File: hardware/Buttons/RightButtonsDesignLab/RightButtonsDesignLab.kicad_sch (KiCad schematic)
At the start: 5 parts, among them J1 Conn_01x03, J2 Conn_01x01, SW1 SW_Push, SW2 SW_Push, SW3 SW_Push

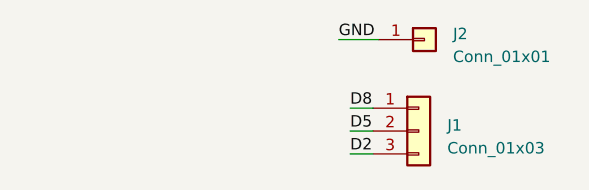
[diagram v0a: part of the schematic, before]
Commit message: BOM of buttons generated
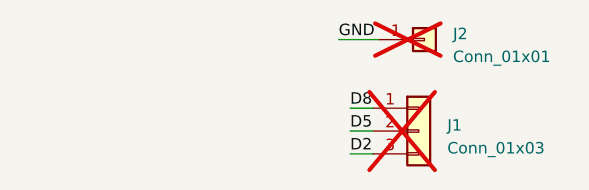
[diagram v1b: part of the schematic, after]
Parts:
- J1, J2: now not fitted
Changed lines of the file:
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@@
   )
   (symbol (lib_id "Connector_Generic:Conn_01x03") (at 189.23 33.655 0) (unit 1)
-    (in_bom yes) (on_board yes) (dnp no) (fields_autoplaced)
+    (in_bom yes) (on_board yes) (dnp yes) (fields_autoplaced)
     (property "Reference" "J1" (at 192.405 33.02 0)
       (effects (font (size 1.27 1.27)) (justify left))
@@
   )
   (symbol (lib_id "Connector_Generic:Conn_01x01") (at 189.865 23.495 0) (unit 1)
-    (in_bom yes) (on_board yes) (dnp no) (fields_autoplaced)
+    (in_bom yes) (on_board yes) (dnp yes) (fields_autoplaced)
     (property "Reference" "J2" (at 193.04 22.86 0)
       (effects (font (size 1.27 1.27)) (justify left))

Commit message: Update all PCB and schematics
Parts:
- removed J1: Conn_01x03, Connector_PinHeader_2.54mm:PinHeader_1x03_P2.54mm_Vertical, symbol Connector_Generic:Conn_01x03
- removed J2: Conn_01x01, Connector_PinHeader_2.54mm:PinHeader_1x01_P2.54mm_Vertical, symbol Connector_Generic:Conn_01x01
- added J1: Conn_01x04, Design:JST_S4B-PH-K-S_LF__SN_, symbol Connector_Generic:Conn_01x04
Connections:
- net D2: now also J1.3 (Pin_3)
- net D5: now also J1.2 (Pin_2)
- net D8: now also J1.1 (Pin_1)
- net GND: now also J1.4 (Pin_4)
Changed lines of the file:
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@@
 (kicad_sch (version 20230121) (generator eeschema)
   (paper "A4")
-  (wire (pts (xy 180.34 23.495) (xy 184.785 23.495))
+  (wire (pts (xy 27.94 37.465) (xy 34.29 37.465))
     (stroke (width 0) (type default))
   )
-  (wire (pts (xy 27.94 37.465) (xy 34.29 37.465))
+  (wire (pts (xy 181.61 38.1) (xy 185.42 38.1))
+    (stroke (width 0) (type default))
+  )
+  (wire (pts (xy 181.61 33.02) (xy 185.42 33.02))
     (stroke (width 0) (type default))
   )
@@
     (stroke (width 0) (type default))
   )
-  (wire (pts (xy 181.61 33.655) (xy 184.15 33.655))
+  (wire (pts (xy 69.215 37.465) (xy 75.565 37.465))
     (stroke (width 0) (type default))
   )
-  (wire (pts (xy 69.215 37.465) (xy 75.565 37.465))
+  (wire (pts (xy 181.61 35.56) (xy 185.42 35.56))
     (stroke (width 0) (type default))
   )
@@
     (stroke (width 0) (type default))
   )
-  (wire (pts (xy 181.61 31.115) (xy 184.15 31.115))
-    (stroke (width 0) (type default))
-  )
-  (wire (pts (xy 181.61 36.195) (xy 184.15 36.195))
+  (wire (pts (xy 181.61 40.64) (xy 185.42 40.64))
     (stroke (width 0) (type default))
   )
@@
     (effects (font (size 1.27 1.27)) (justify left bottom))
   )
-  (label "GND" (at 27.94 37.465 0) (fields_autoplaced)
+  (label "D2" (at 181.61 38.1 0) (fields_autoplaced)
     (effects (font (size 1.27 1.27)) (justify left bottom))
   )
-  (label "GND" (at 180.34 23.495 0) (fields_autoplaced)
+  (label "D5" (at 181.61 35.56 0) (fields_autoplaced)
     (effects (font (size 1.27 1.27)) (justify left bottom))
   )
-  (label "D2" (at 181.61 36.195 0) (fields_autoplaced)
+  (label "GND" (at 27.94 37.465 0) (fields_autoplaced)
     (effects (font (size 1.27 1.27)) (justify left bottom))
   )
@@
     (effects (font (size 1.27 1.27)) (justify left bottom))
   )
-  (label "D5" (at 181.61 33.655 0) (fields_autoplaced)
-    (effects (font (size 1.27 1.27)) (justify left bottom))
-  )
   (label "D2" (at 46.99 37.465 0) (fields_autoplaced)
     (effects (font (size 1.27 1.27)) (justify left bottom))
   )
-  (label "D8" (at 181.61 31.115 0) (fields_autoplaced)
+  (label "D8" (at 125.095 37.465 0) (fields_autoplaced)
     (effects (font (size 1.27 1.27)) (justify left bottom))
   )
-  (label "D8" (at 125.095 37.465 0) (fields_autoplaced)
+  (label "D8" (at 181.61 33.02 0) (fields_autoplaced)
+    (effects (font (size 1.27 1.27)) (justify left bottom))
+  )
+  (label "GND" (at 181.61 40.64 0) (fields_autoplaced)
     (effects (font (size 1.27 1.27)) (justify left bottom))
   )
@@
     )
   )
-  (symbol (lib_id "Connector_Generic:Conn_01x03") (at 189.23 33.655 0) (unit 1)
-    (in_bom yes) (on_board yes) (dnp yes) (fields_autoplaced)
-    (property "Reference" "J1" (at 192.405 33.02 0)
-      (effects (font (size 1.27 1.27)) (justify left))
+  (symbol (lib_id "Connector_Generic:Conn_01x04") (at 190.5 35.56 0) (unit 1)
+    (in_bom yes) (on_board yes) (dnp no)
+    (property "Reference" "J1" (at 190.5 46.355 0)
+      (effects (font (size 1.27 1.27)))
     )
-    (property "Value" "Conn_01x03" (at 192.405 35.56 0)
-      (effects (font (size 1.27 1.27)) (justify left))
+    (property "Value" "Conn_01x04" (at 190.5 43.815 0)
+      (effects (font (size 1.27 1.27)))
     )
-    (property "Footprint" "Connector_PinHeader_2.54mm:PinHeader_1x03_P2.54mm_Vertical" (at 189.23 33.655 0)
+    (property "Footprint" "Design:JST_S4B-PH-K-S_LF__SN_" (at 190.5 35.56 0)
       (effects (font (size 1.27 1.27)) hide)
     )
-    (property "Datasheet" "~" (at 189.23 33.655 0)
+    (property "Datasheet" "https://datasheet.lcsc.com/lcsc/2304140030_JST-S4B-PH-K-S-LF-SN_C157926.pdf" (at 190.5 35.56 0)
+      (effects (font (size 1.27 1.27)) hide)
+    )
+    (property "LCSC#" "C157926" (at 190.5 35.56 0)
       (effects (font (size 1.27 1.27)) hide)
     )
@@
     (pin "2")
     (pin "3")
+    (pin "4")
     (instances
       (project "RightButtonsDesignLab"
@@
         )
       )
-      (project "ButtonDesignLab"
-        (path "/e63e39d7-6ac0-4ffd-8aa3-1841a4541b55"
-          (reference "J2") (unit 1)
-        )
-      )
-    )
-  )
-  (symbol (lib_id "Connector_Generic:Conn_01x01") (at 189.865 23.495 0) (unit 1)
-    (in_bom yes) (on_board yes) (dnp yes) (fields_autoplaced)
-    (property "Reference" "J2" (at 193.04 22.86 0)
-      (effects (font (size 1.27 1.27)) (justify left))
-    )
-    (property "Value" "Conn_01x01" (at 193.04 25.4 0)
-      (effects (font (size 1.27 1.27)) (justify left))
-    )
-    (property "Footprint" "Connector_PinHeader_2.54mm:PinHeader_1x01_P2.54mm_Vertical" (at 189.865 23.495 0)
-      (effects (font (size 1.27 1.27)) hide)
-    )
-    (property "Datasheet" "~" (at 189.865 23.495 0)
-      (effects (font (size 1.27 1.27)) hide)
-    )
-    (pin "1")
-    (instances
-      (project "RightButtonsDesignLab"
-        (path "/d8ab91b7-7f4a-4c3a-afb3-beb7d8cda53a"
-          (reference "J2") (unit 1)
-        )
-      )
-      (project "ButtonDesignLab"
-        (path "/e63e39d7-6ac0-4ffd-8aa3-1841a4541b55"
-          (reference "J7") (unit 1)
-        )
-      )

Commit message: Update PCB
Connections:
- net D2: now also J1.2 (Pin_2); no longer J1.3 (Pin_3)
- net D5: now also J1.3 (Pin_3); no longer J1.2 (Pin_2)
- net D8: now also J1.4 (Pin_4); no longer J1.1 (Pin_1)
- net GND: now also J1.1 (Pin_1); no longer J1.4 (Pin_4)
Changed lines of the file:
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@@
     )
   )
-  (symbol (lib_id "Connector_Generic:Conn_01x04") (at 190.5 35.56 0) (unit 1)
+  (symbol (lib_id "Connector_Generic:Conn_01x04") (at 190.5 38.1 0) (mirror x) (unit 1)
     (in_bom yes) (on_board yes) (dnp no)
-    (property "Reference" "J1" (at 190.5 46.355 0)
+    (property "Reference" "J1" (at 190.5 27.305 0)
       (effects (font (size 1.27 1.27)))
     )
-    (property "Value" "Conn_01x04" (at 190.5 43.815 0)
+    (property "Value" "Conn_01x04" (at 190.5 29.845 0)
       (effects (font (size 1.27 1.27)))
     )
-    (property "Footprint" "Design:JST_S4B-PH-K-S_LF__SN_" (at 190.5 35.56 0)
+    (property "Footprint" "Design:JST_S4B-PH-K-S_LF__SN_" (at 190.5 38.1 0)
       (effects (font (size 1.27 1.27)) hide)
     )
-    (property "Datasheet" "https://datasheet.lcsc.com/lcsc/2304140030_JST-S4B-PH-K-S-LF-SN_C157926.pdf" (at 190.5 35.56 0)
+    (property "Datasheet" "https://datasheet.lcsc.com/lcsc/2304140030_JST-S4B-PH-K-S-LF-SN_C157926.pdf" (at 190.5 38.1 0)
       (effects (font (size 1.27 1.27)) hide)
     )
-    (property "LCSC#" "C157926" (at 190.5 35.56 0)
+    (property "LCSC#" "C157926" (at 190.5 38.1 0)
       (effects (font (size 1.27 1.27)) hide)
     )
